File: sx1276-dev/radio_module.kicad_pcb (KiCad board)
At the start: 2 copper layers, 112 parts, among them IC1 GRF5112, IC2 GRF5112, J1 Conn_Coaxial, J2 Conn_Coaxial, J3 Conn_01x08_Socket, J4 Conn_01x08_Socket, U1 TQP3M9036, U2 4259-63, U3 NC7SZ04P5X, U4 SX1276IMLTRT, U5 4259-63, U6 TQP3M9036

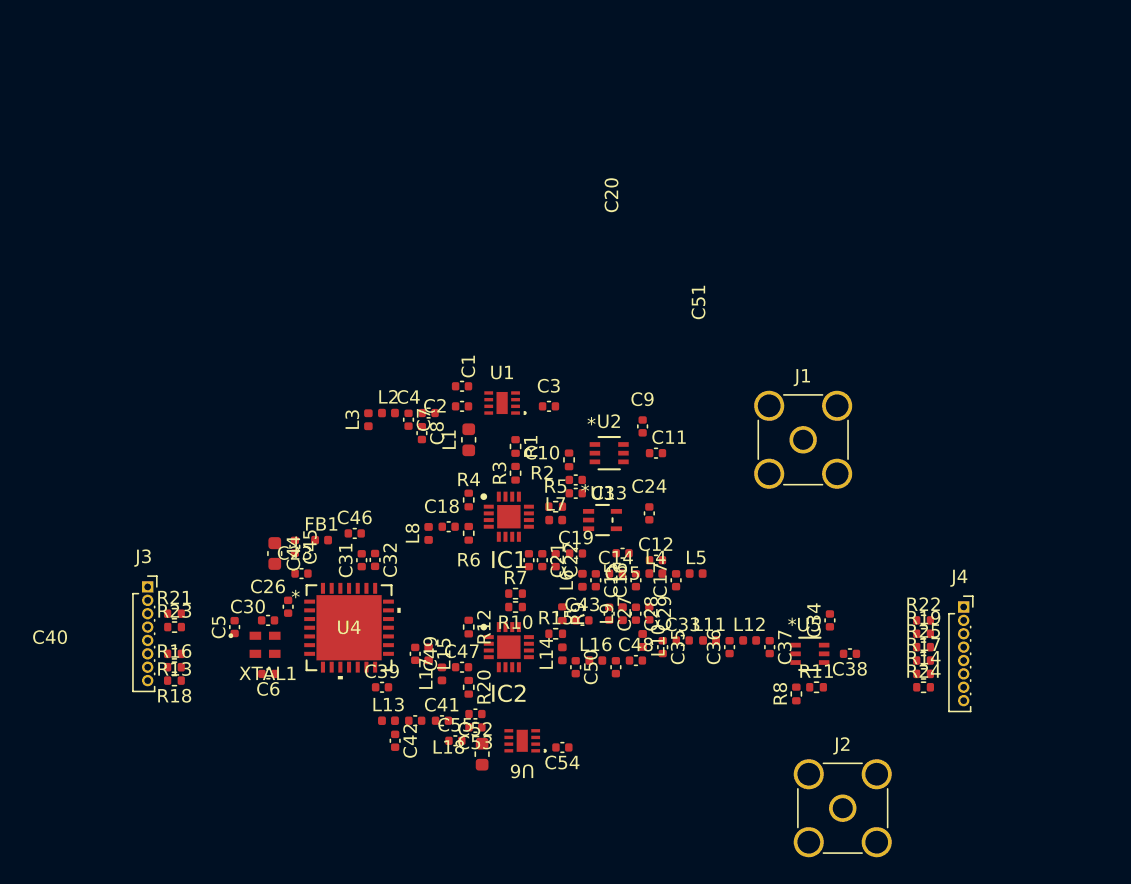
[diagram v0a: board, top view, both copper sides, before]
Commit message: Updated Schematic and continued layout
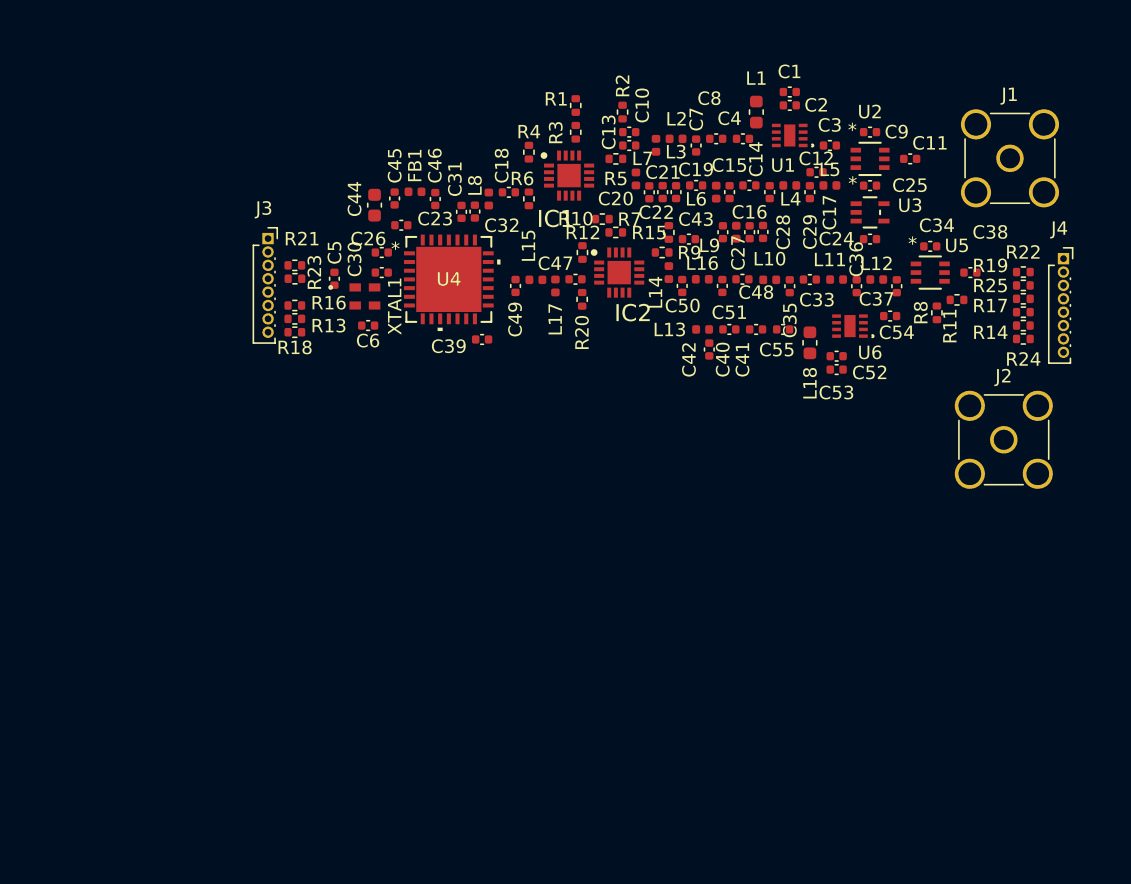
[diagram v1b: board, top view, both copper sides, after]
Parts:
- moved C54 40.5 mm to (146.0, 107.3)
- moved U6 39.5 mm to (143.0, 108.0)
- moved C55 39.3 mm to (138.0, 108.3)
- moved L18 39.3 mm to (140.0, 109.3)
- moved C53 38.7 mm to (142.0, 110.3), turned to 0 degrees
- moved C40 37.5 mm to (134.0, 108.3)
- moved C41 37.5 mm to (136.0, 108.3)
- moved C42 37.5 mm to (132.5, 109.8)
- moved L13 37.5 mm to (132.0, 108.3)
- moved C52 37.3 mm to (142.0, 111.3), turned to 0 degrees
- moved C2 33.3 mm to (138.5, 91.5), turned to 0 degrees
- moved C25 33.1 mm to (144.5, 97.5), turned to 180 degrees
- moved C1 32.9 mm to (138.5, 90.5), turned to 0 degrees
- moved L1 32.6 mm to (136.0, 92.0), turned to -90 degrees
- moved C12 31.4 mm to (140.5, 96.5)
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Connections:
- net Net-(U2-RF2) renamed RF_LF_SW
- net Net-(U5-RF1) renamed RF_HF_SW
- L10 pad 1: Net-(C33-Pad1) -> HF_PA_OUT
- L10 pad 2: HF_PA_OUT -> Net-(C33-Pad1)

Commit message: Made adjustments to layout
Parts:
- removed J1, J2: Conn_Coaxial, Connector_Coaxial:SMA_Amphenol_901-144_Vertical
- moved C44 4.97 mm to (102.5, 99.0)
- moved C45 4.97 mm to (104.0, 98.5)
- moved C46 4.97 mm to (107.0, 98.5)
- moved FB1 4.97 mm to (105.5, 98.0)
- moved J4 2.22 mm to (160.0, 101.0)
- moved R14 2.22 mm to (157.0, 106.0)
- moved R17 2.22 mm to (157.0, 105.0)
- moved R19 2.22 mm to (157.0, 103.0)
- moved R22 2.22 mm to (157.0, 102.0)
- moved R24 2.22 mm to (157.0, 107.0)
- moved R25 2.22 mm to (157.0, 104.0)
- moved C23 2.11 mm to (108.0, 102.0)
- moved R21 1.96 mm to (101.5, 101.5)
- moved J3 1.96 mm to (99.5, 99.5)
- moved R13 1.96 mm to (101.5, 104.5)
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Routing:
- added copper zone on In1.Cu, net GND
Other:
- copper layers 2 -> 4

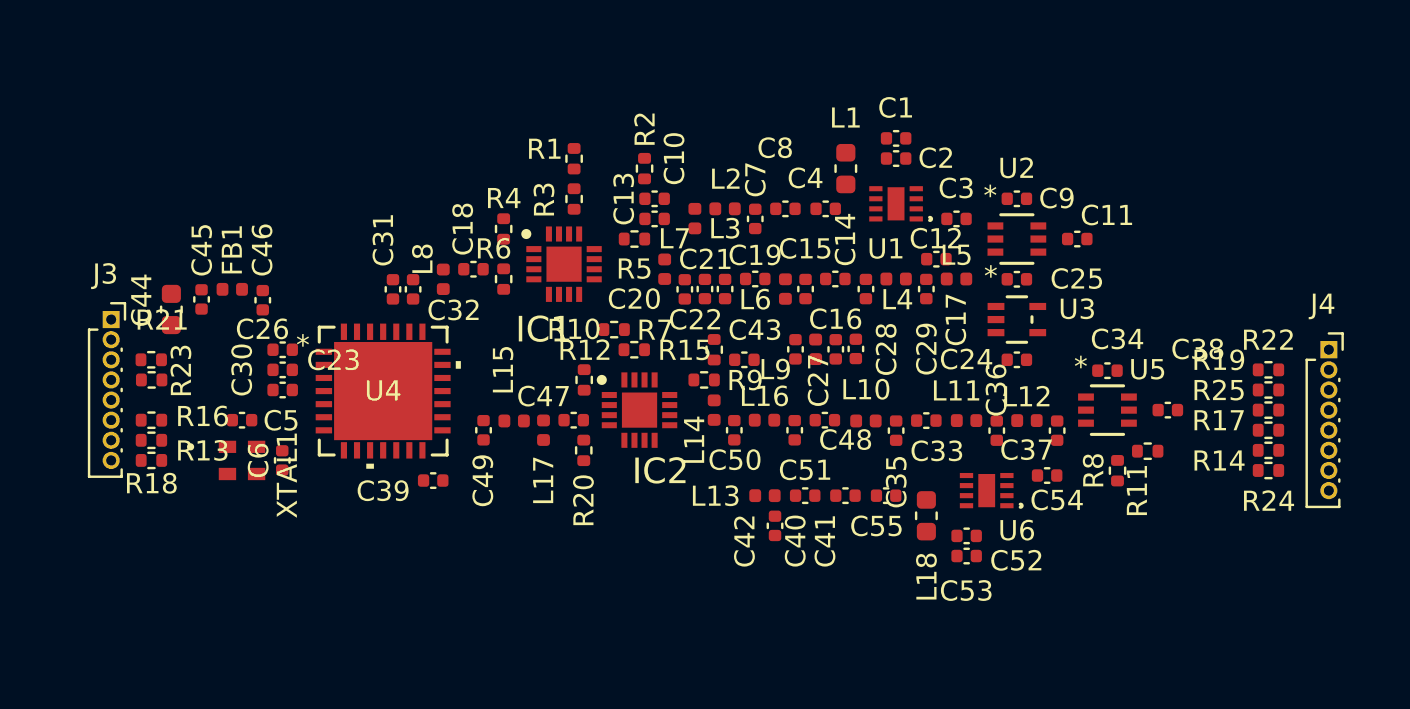
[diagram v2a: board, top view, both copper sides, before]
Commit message: Added routing to pcb
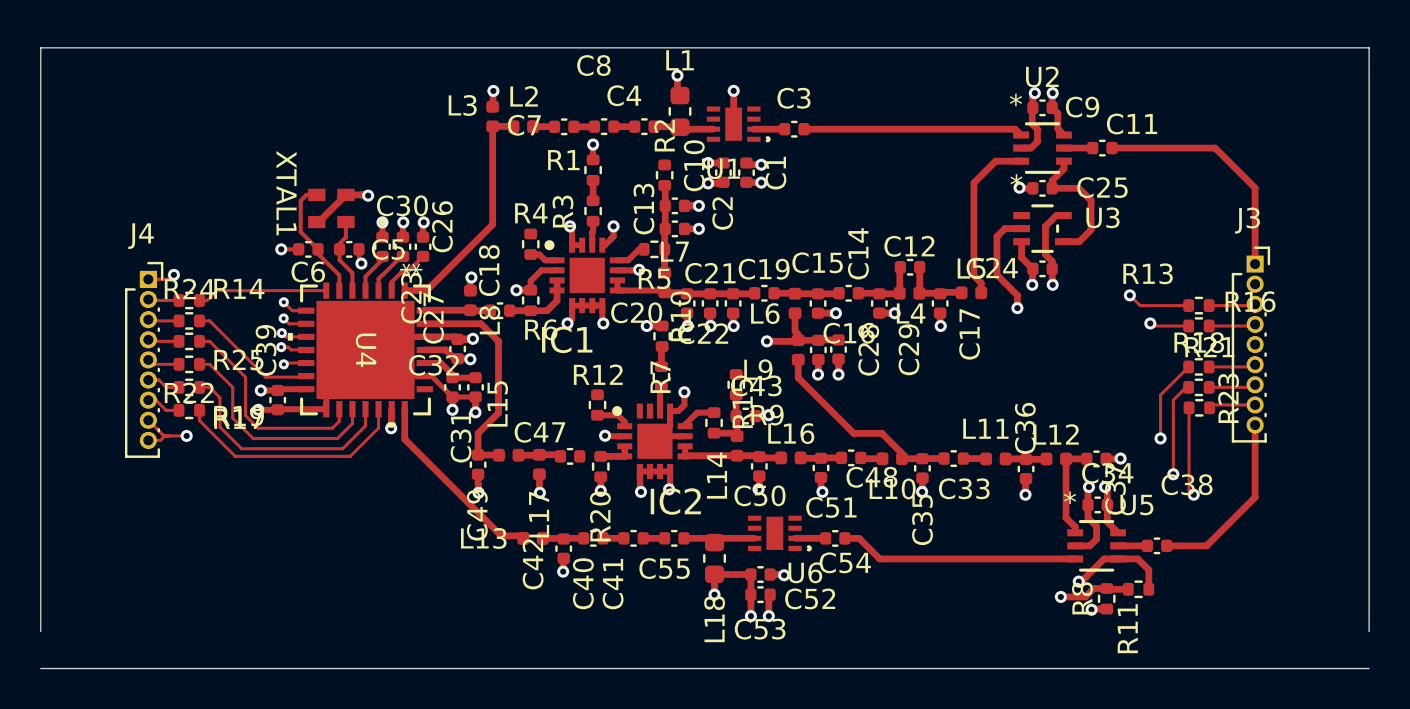
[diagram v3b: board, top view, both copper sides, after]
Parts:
- removed C44: 22uF, Capacitor_SMD:C_0603_1608Metric
- removed C45, C46: 1uF, Capacitor_SMD:C_0402_1005Metric
- removed FB1: FerriteBead, Inductor_SMD:L_0402_1005Metric
- J3, J4: value Conn_01x08_Socket -> Conn_01x09_Pin; footprint Connector_PinSocket_1.00mm:PinSocket_1x08_P1.00mm_Vertical -> Connector_PinSocket_1.00mm:PinSocket_1x09_P1.00mm_Vertical
- moved J4 58.8 mm to (101.3, 97.5)
- moved J3 56.9 mm to (156.3, 96.7)
- moved R14 54.1 mm to (103.4, 98.6), turned to 180 degrees
- moved R24 54.1 mm to (103.4, 99.6), turned to 180 degrees
- moved R25 53.7 mm to (103.4, 100.6), turned to 180 degrees
- moved R17 53.6 mm to (103.4, 104.0), turned to 180 degrees
- moved R22 53.6 mm to (103.4, 101.7), turned to 180 degrees
- moved R19 53.6 mm to (103.4, 102.9), turned to 180 degrees
- moved R13 52.4 mm to (153.5, 98.8), turned to 0 degrees
- moved R16 52.4 mm to (153.5, 99.8)
- moved R18 52.2 mm to (153.5, 101.9), turned to 0 degrees
- moved R23 52.1 mm to (153.6, 103.9)
- moved R21 52.1 mm to (153.5, 102.9)
- moved C27 16.8 mm to (116.7, 101.0), turned to 90 degrees
- moved XTAL1 13.3 mm to (110.4, 94.0), turned to 180 degrees
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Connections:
- C1 pad 1: +3.3VA -> +3V3
- C11 pad 2: Net-(J1-In) -> /ANT1
- C2 pad 1: +3.3VA -> +3V3
- C24 pad 1: +3.3VA -> +3V3
- C34 pad 1: +3.3VA -> +3V3
- C38 pad 1: Net-(J2-In) -> /ANT2
- C52 pad 1: +3.3VA -> +3V3
- C53 pad 1: +3.3VA -> +3V3
- C9 pad 1: +3.3VA -> +3V3
- J3 pad 1: /ANT -> /ANT1
- J3 pad 3: /DIO3 -> /DIO0
- J3 pad 4: /DIO4 -> /DIO1
- J3 pad 6: /DIO0 -> /DIO2
- J3 pad 7: /DIO1 -> /DIO3
- J3 pad 8: /DIO2 -> /DIO4
- J4 pad 2: /MISO -> /NRESET
- J4 pad 3: /MOSI -> /DIO5
- J4 pad 5: /NSS -> /MISO
- J4 pad 6: /NRESET -> /MOSI
- J4 pad 7: /DIO5 -> /NSS
- L1 pad 1: +3.3VA -> +3V3
- L18 pad 1: +3.3VA -> +3V3
- R8 pad 1: +3.3VA -> +3V3
- U2 pad 6: +3.3VA -> +3V3
- U3 pad 5: +3.3VA -> +3V3
- U5 pad 6: +3.3VA -> +3V3
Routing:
- net GND: track 0.00 -> 90.2 mm, vias 0 -> 54
- net /DIO2_sx: track 0.00 -> 82.1 mm, vias 0 -> 2
- net /DIO3_sx: track 0.00 -> 77.6 mm, vias 0 -> 2
- net /DIO4_sx: track 0.00 -> 71.9 mm, vias 0 -> 2
- net /DIO1_sx: track 0.00 -> 70.3 mm, vias 0 -> 2
- net /DIO0_sx: track 0.00 -> 67.6 mm, vias 0 -> 2
- net RF_CONTROL: track 0.00 -> 42.0 mm, vias 0 -> 2
- net +3V3: track 0.00 -> 27.6 mm, vias 0 -> 11
- net RF_CONTROL_SW: track 0.00 -> 26.3 mm, vias 0 -> 2
- net VR_PA: track 0.00 -> 22.7 mm, vias 0 -> 2
- net RFI_HF_LNA_IN: track 0.00 -> 11.9 mm
- net /ANT1: track 0.00 -> 11.7 mm
- net /NSS_sx: track 0.00 -> 11.7 mm
- net /MOSI_sx: track 0.00 -> 11.7 mm
- net RFI_LF: track 0.00 -> 11.4 mm
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- added copper zone on In2.Cu, net +3V3
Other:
- board outline added: 66 x 30.8 mm

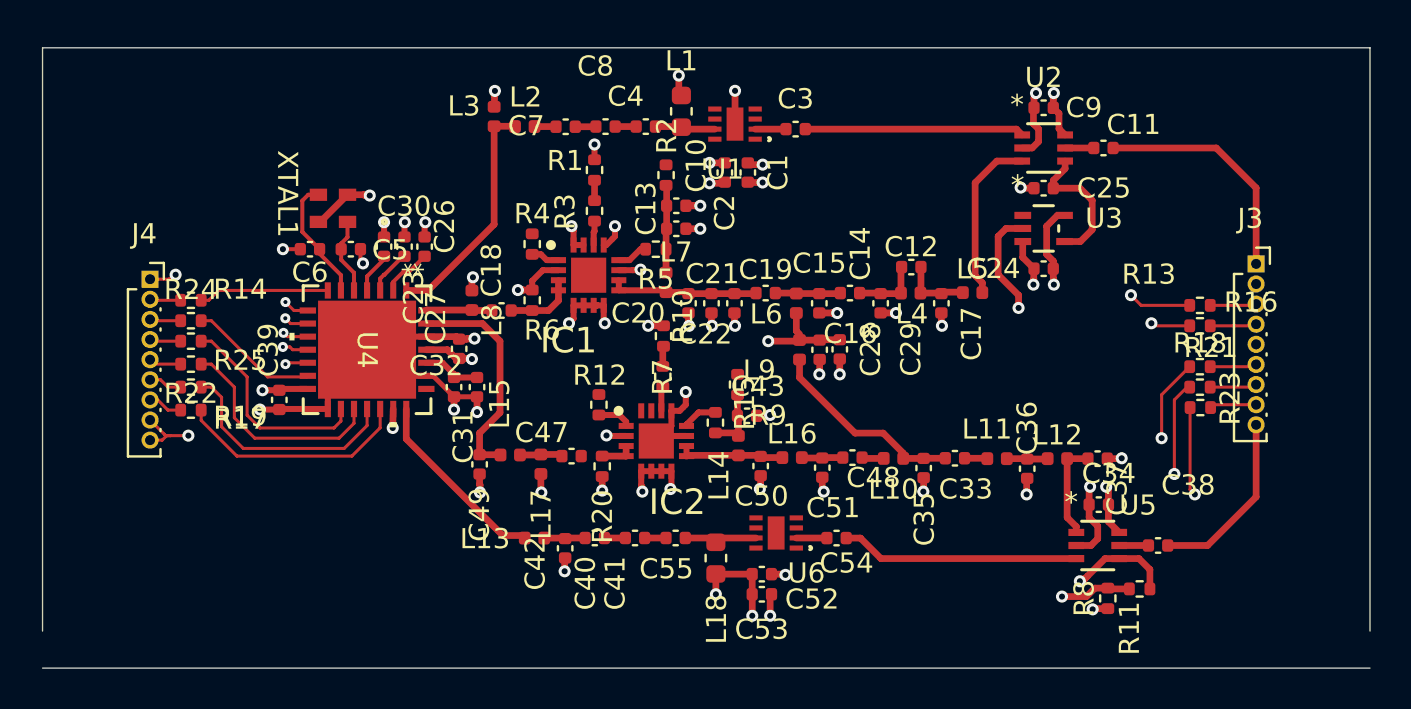
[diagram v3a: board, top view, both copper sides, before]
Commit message: fixed routing and attempted via fencing
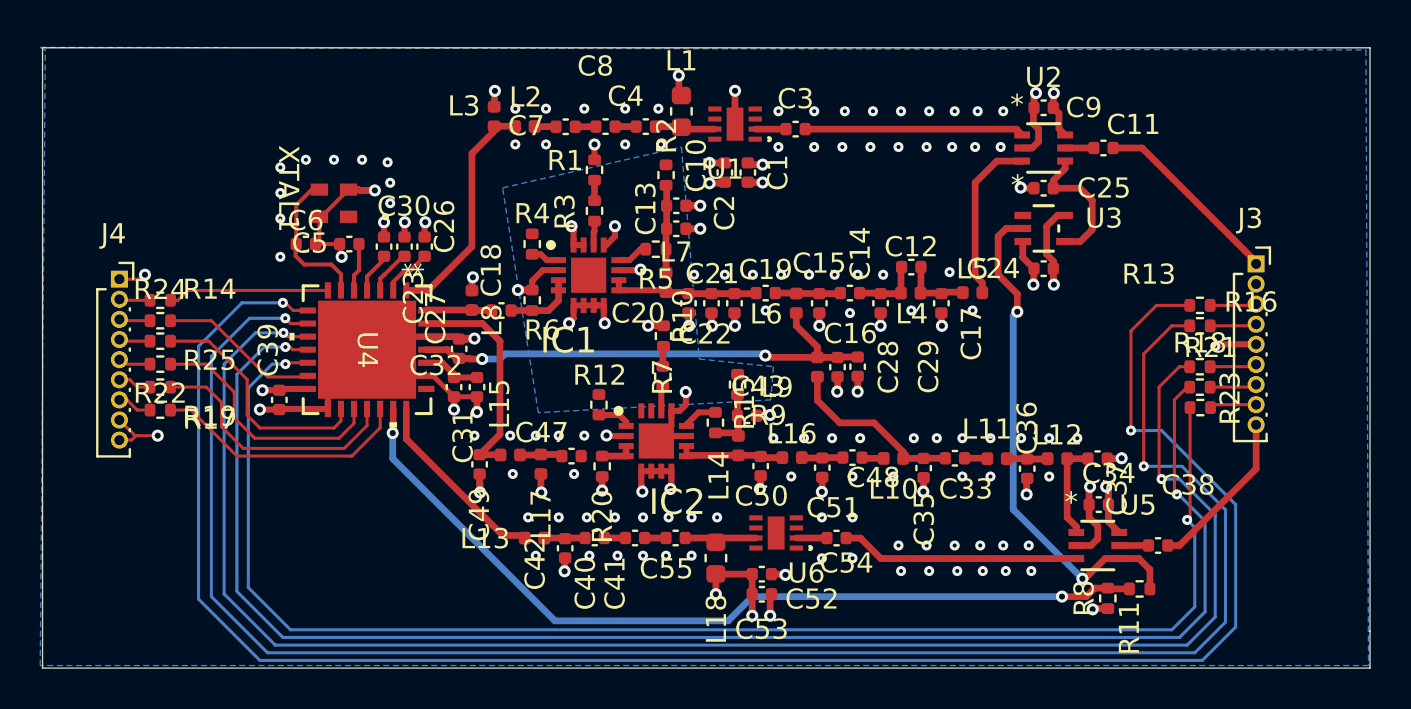
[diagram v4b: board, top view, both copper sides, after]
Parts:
- moved J4 1.52 mm to (99.8, 97.5)
- moved R14 1.52 mm to (101.9, 98.6)
- moved R17 1.52 mm to (101.9, 104.0)
- moved R19 1.52 mm to (101.9, 102.9)
- moved R22 1.52 mm to (101.9, 101.7)
- moved R24 1.52 mm to (101.9, 99.6)
- moved R25 1.52 mm to (101.9, 100.6)
- moved C29 1.24 mm to (136.5, 101.9)
- moved C28 1.24 mm to (135.5, 101.9)
- moved L9 1.24 mm to (134.5, 101.9)
- moved C6 0.33 mm to (109.1, 95.8), turned to 0 degrees
- moved C5 0.27 mm to (111.3, 95.8), turned to 180 degrees
- moved XTAL1 0.26 mm to (110.5, 93.7)
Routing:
- net /DIO0_sx: track 67.6 -> 93.8 mm
- net /DIO1_sx: track 70.3 -> 89.2 mm
- net +5V: track 0.00 -> 2.38 mm, vias 0 -> 1
- net /ANT1: track 11.7 -> 9.55 mm
- net VR_PA: track 22.7 -> 24.5 mm
- net RF_CONTROL: track 42.0 -> 43.6 mm
- net /NRESET_sx: track 6.50 -> 8.02 mm
- net /DIO5_sx: track 6.48 -> 8.00 mm
- net /SCK_sx: track 10.6 -> 12.0 mm
- net XTA: track 3.80 -> 2.41 mm
- net /MISO_sx: track 11.0 -> 12.4 mm
- net /MOSI_sx: track 11.7 -> 13.0 mm
- net XTB: track 6.18 -> 7.45 mm
- net /NSS_sx: track 11.7 -> 12.9 mm
- net RF_CONTROL_SW: track 26.3 -> 25.3 mm
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- added copper zone on B.Cu, net +5V
- added copper zone on B.Cu, net GND
